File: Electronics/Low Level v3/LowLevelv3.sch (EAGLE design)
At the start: 66 parts, among them IC1_2515 MCP2515, IC2_2551 MCP2551DIL08, IC3_4802 MCP4802, Q1 16MHz, T1 2N3904, T2 2N3904, X1 284512-4, X3 Motor, X4 CLICK

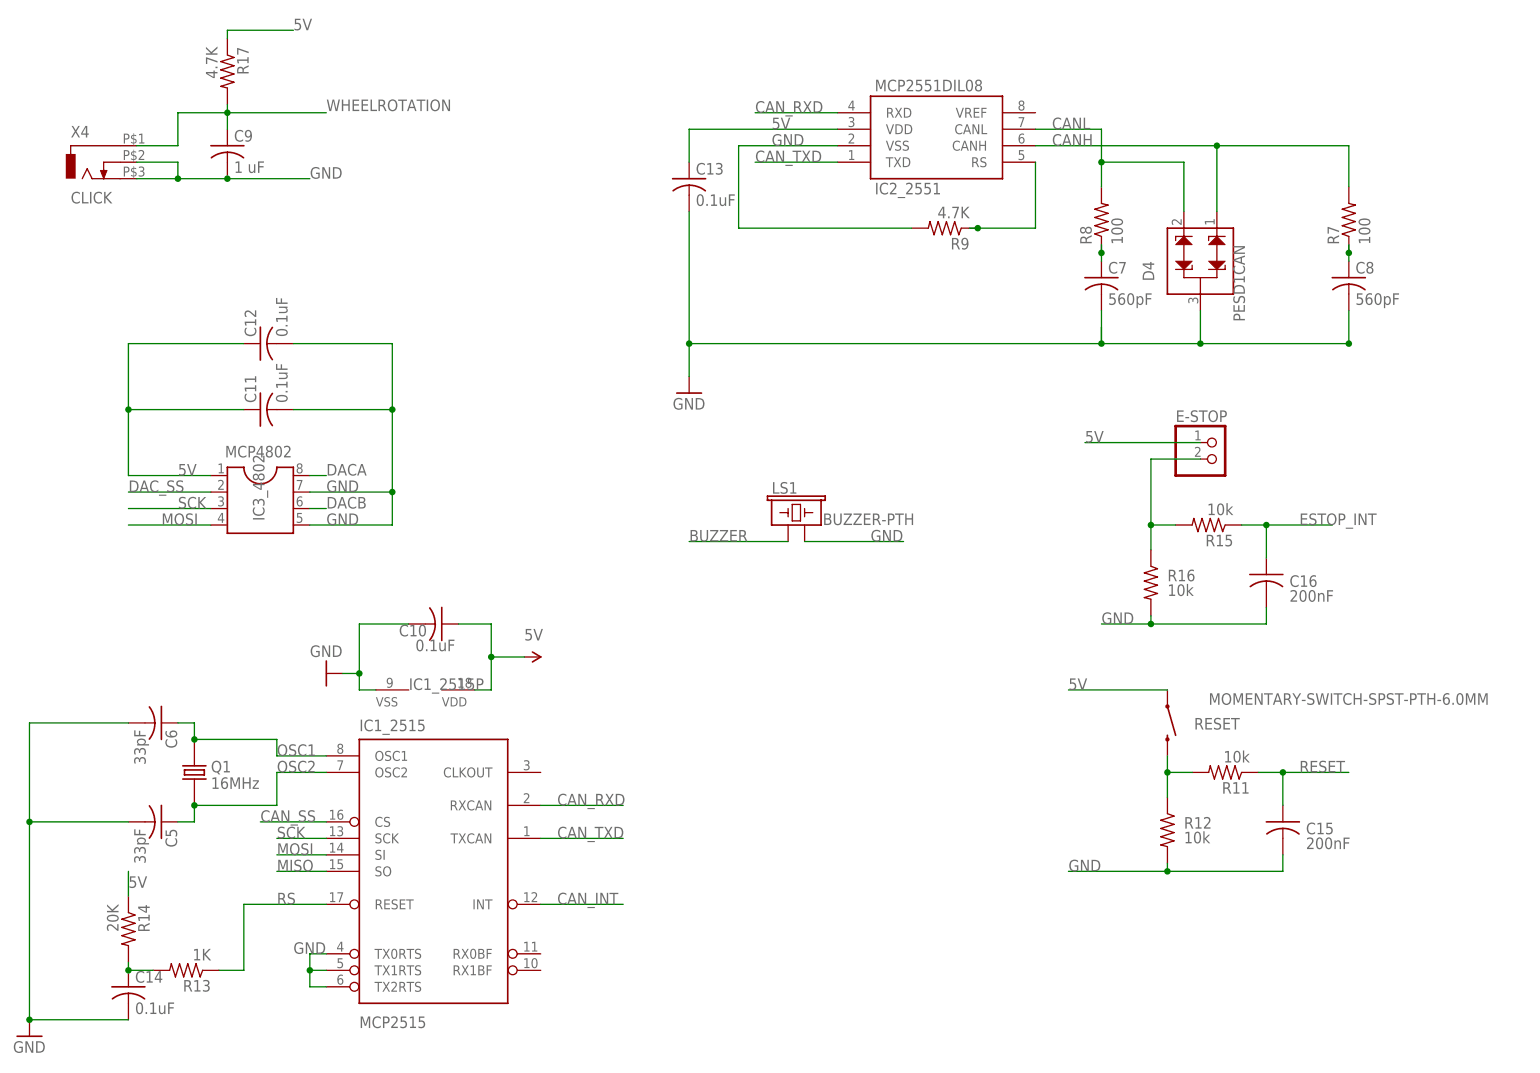
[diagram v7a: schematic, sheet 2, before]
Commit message: swapped 0.2uF for 0.1uF, updated BoM
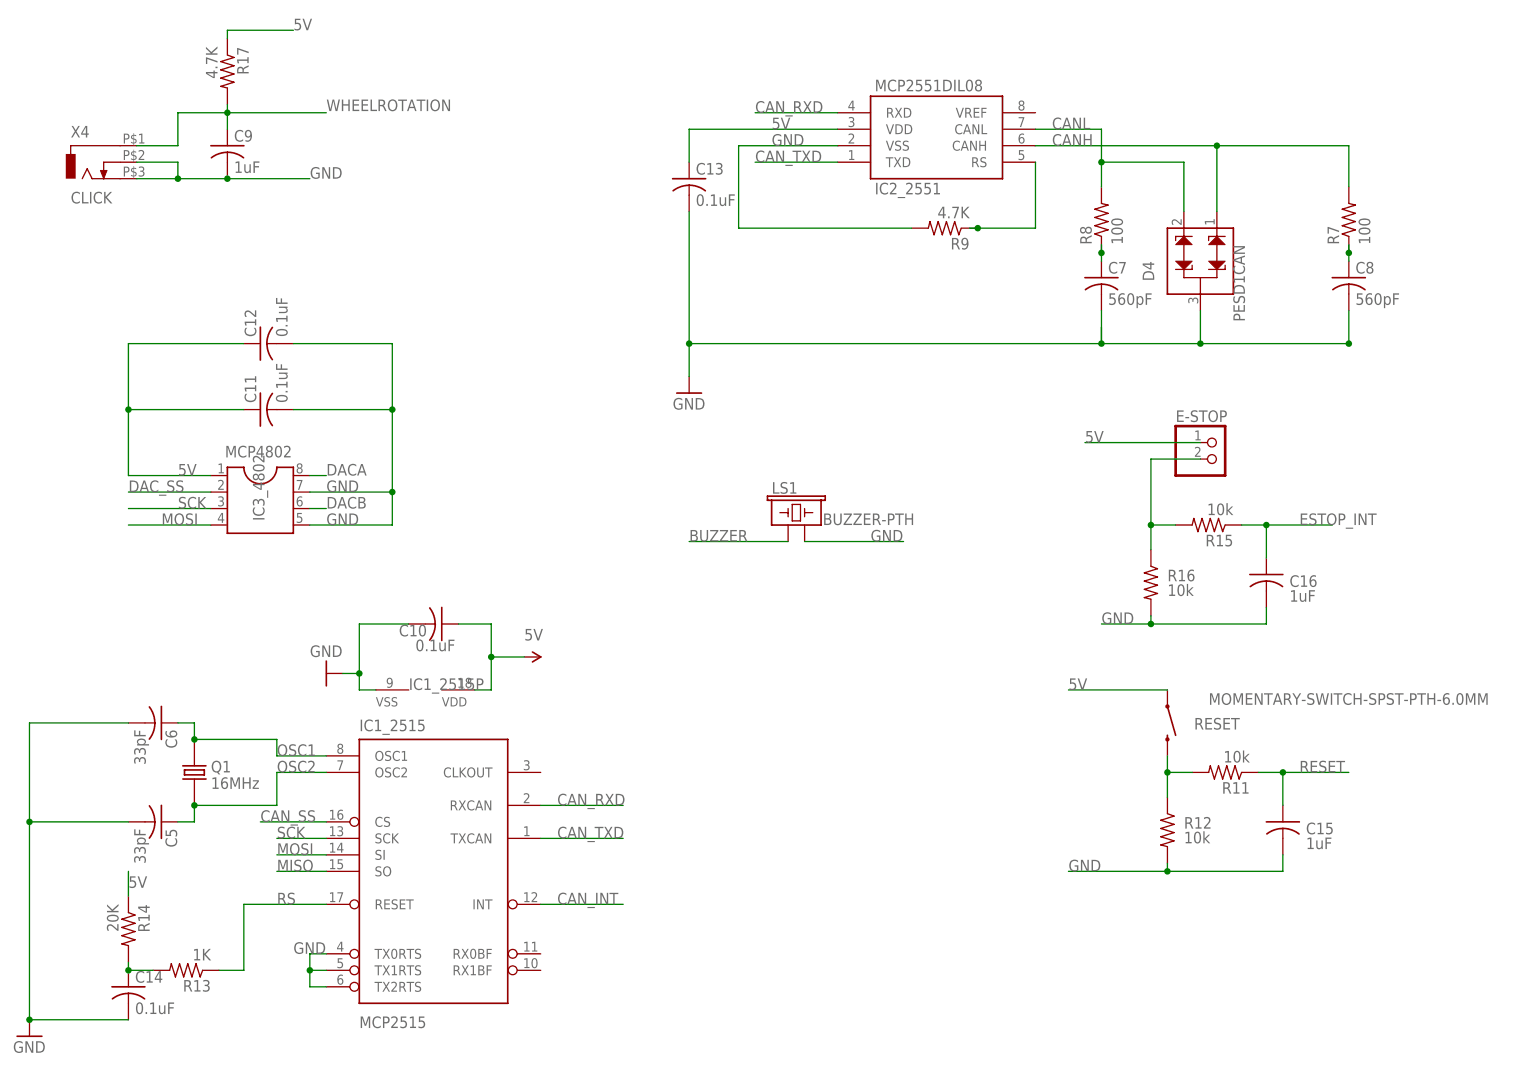
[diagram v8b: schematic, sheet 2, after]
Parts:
- C15, C16: value 200nF -> 1uF
- C9: value 1 uF -> 1uF
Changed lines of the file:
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@@
 <part name="X3" library="con-subd" library_urn="urn:adsk.eagle:library:189" deviceset="M15" device="-182" package3d_urn="urn:adsk.eagle:package:10309/1" value="Motor"/>
 <part name="C11" library="resistor" library_urn="urn:adsk.eagle:library:348" deviceset="C-US" device="C1206" package3d_urn="urn:adsk.eagle:package:23618/2" value="0.1uF"/>
-<part name="C9" library="resistor" library_urn="urn:adsk.eagle:library:348" deviceset="C-US" device="C1206" package3d_urn="urn:adsk.eagle:package:23618/2" value="1 uF"/>
+<part name="C9" library="resistor" library_urn="urn:adsk.eagle:library:348" deviceset="C-US" device="C1206" package3d_urn="urn:adsk.eagle:package:23618/2" value="1uF"/>
 <part name="X4" library="elcanoParts" deviceset="ODO_JACK" device="" value="CLICK"/>
 <part name="C2" library="resistor" library_urn="urn:adsk.eagle:library:348" deviceset="C-US" device="C1206" package3d_urn="urn:adsk.eagle:package:23618/2" value="1uF"/>
@@
 <part name="R14" library="resistor" library_urn="urn:adsk.eagle:library:348" deviceset="R-US_" device="R1206" package3d_urn="urn:adsk.eagle:package:23540/2" value="20K"/>
 <part name="LS1" library="SparkFun-Electromechanical" library_urn="urn:adsk.eagle:library:516" deviceset="BUZZER" device="-PTH" package3d_urn="urn:adsk.eagle:package:38558/1"/>
-<part name="C15" library="resistor" library_urn="urn:adsk.eagle:library:348" deviceset="C-US" device="C1206" package3d_urn="urn:adsk.eagle:package:23618/2" value="200nF"/>
+<part name="C15" library="resistor" library_urn="urn:adsk.eagle:library:348" deviceset="C-US" device="C1206" package3d_urn="urn:adsk.eagle:package:23618/2" value="1uF"/>
 <part name="R12" library="resistor" library_urn="urn:adsk.eagle:library:348" deviceset="R-US_" device="R1206" package3d_urn="urn:adsk.eagle:package:23540/2" value="10k"/>
 <part name="E-STOP" library="pinhead" library_urn="urn:adsk.eagle:library:325" deviceset="PINHD-1X2" device="" package3d_urn="urn:adsk.eagle:package:22435/2"/>
 <part name="R15" library="resistor" library_urn="urn:adsk.eagle:library:348" deviceset="R-US_" device="R1206" package3d_urn="urn:adsk.eagle:package:23540/2" value="10k"/>
 <part name="R16" library="resistor" library_urn="urn:adsk.eagle:library:348" deviceset="R-US_" device="R1206" package3d_urn="urn:adsk.eagle:package:23540/2" value="10k"/>
-<part name="C16" library="resistor" library_urn="urn:adsk.eagle:library:348" deviceset="C-US" device="C1206" package3d_urn="urn:adsk.eagle:package:23618/2" value="200nF"/>
+<part name="C16" library="resistor" library_urn="urn:adsk.eagle:library:348" deviceset="C-US" device="C1206" package3d_urn="urn:adsk.eagle:package:23618/2" value="1uF"/>
 <part name="R17" library="resistor" library_urn="urn:adsk.eagle:library:348" deviceset="R-US_" device="R1206" package3d_urn="urn:adsk.eagle:package:23540/2" value="4.7K"/>
 </parts>
